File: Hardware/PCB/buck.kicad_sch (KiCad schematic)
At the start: 13 parts, among them J4 54-00127, U4 LMR33630BRNXR

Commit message: swapped to be better precision resistors for feedback on buck and votlage reference for ADCs
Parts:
- R10: footprint Capacitor_SMD:C_0402_1005Metric_Pad0.74x0.62mm_HandSolder -> Capacitor_SMD:C_0603_1608Metric_Pad1.08x0.95mm_HandSolder; DigiKey Link https://www.digikey.com/en/products/detail/yageo/RC0402FR-0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 -> https://www.digikey.com/en/products/detail/susumu/RG1608P-2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; MPN RC0402FR-0722K1L -> RG1608P-2212-B-T5; Manufacturer YAGEO -> Susumu
- R9: footprint Capacitor_SMD:C_0402_1005Metric_Pad0.74x0.62mm_HandSolder -> Capacitor_SMD:C_0603_1608Metric_Pad1.08x0.95mm_HandSolder; DigiKey Link https://www.digikey.com/en/products/detail/yageo/RC0402FR-0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 -> https://www.digikey.com/en/products/detail/susumu/RG1608P-1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; MPN RC0402FR-07100KL -> RG1608P-104-B-T5; Manufacturer YAGEO -> Susumu
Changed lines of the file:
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@@
 			)
 		)
-		(property "Footprint" "Capacitor_SMD:C_0402_1005Metric_Pad0.74x0.62mm_HandSolder"
+		(property "Footprint" "Capacitor_SMD:C_0603_1608Metric_Pad1.08x0.95mm_HandSolder"
 			(at 193.04 95.25 0)
 			(effects
@@
 			)
 		)
-		(property "Description" "100 kOhms ±1% 0.063W, 1/16W Chip Resistor 0402 (1005 Metric) Moisture Resistant Thick Film"
-			(at 193.04 95.25 0)
-			(effects
-				(font
-					(size 1.27 1.27)
-				)
-				(hide yes)
-			)
-		)
-		(property "DigiKey Link" "https://www.digikey.com/en/products/detail/yageo/RC0402FR-07100KL/726526"
-			(at 193.04 95.25 0)
-			(effects
-				(font
-					(size 1.27 1.27)
-				)
-				(hide yes)
-			)
-		)
-		(property "MPN" "RC0402FR-07100KL"
-			(at 193.04 95.25 0)
-			(effects
-				(font
-					(size 1.27 1.27)
-				)
-				(hide yes)
-			)
-		)
-		(property "Manufacturer" "YAGEO"
+		(property "Description" "100 kOhms ±0.1% 0.1W, 1/10W Chip Resistor 0603 (1608 Metric) Anti-Sulfur, Automotive AEC-Q200 Thin Film"
+			(at 193.04 95.25 0)
+			(effects
+				(font
+					(size 1.27 1.27)
+				)
+				(hide yes)
+			)
+		)
+		(property "DigiKey Link" "https://www.digikey.com/en/products/detail/susumu/RG1608P-104-B-T5/1240451"
+			(at 193.04 95.25 0)
+			(effects
+				(font
+					(size 1.27 1.27)
+				)
+				(hide yes)
+			)
+		)
+		(property "MPN" "RG1608P-104-B-T5"
+			(at 193.04 95.25 0)
+			(effects
+				(font
+					(size 1.27 1.27)
+				)
+				(hide yes)
+			)
+		)
+		(property "Manufacturer" "Susumu"
 			(at 193.04 95.25 0)
 			(effects
@@
 			)
 		)
-		(property "Footprint" "Capacitor_SMD:C_0402_1005Metric_Pad0.74x0.62mm_HandSolder"
+		(property "Footprint" "Capacitor_SMD:C_0603_1608Metric_Pad1.08x0.95mm_HandSolder"
 			(at 193.04 105.41 0)
 			(effects
@@
 			)
 		)
-		(property "Description" "22.1 kOhms ±1% 0.063W, 1/16W Chip Resistor 0402 (1005 Metric) Moisture Resistant Thick Film"
-			(at 193.04 105.41 0)
-			(effects
-				(font
-					(size 1.27 1.27)
-				)
-				(hide yes)
-			)
-		)
-		(property "DigiKey Link" "https://www.digikey.com/en/products/detail/yageo/RC0402FR-0722K1L/726563"
-			(at 193.04 105.41 0)
-			(effects
-				(font
-					(size 1.27 1.27)
-				)
-				(hide yes)
-			)
-		)
-		(property "MPN" "RC0402FR-0722K1L"
-			(at 193.04 105.41 0)
-			(effects
-				(font
-					(size 1.27 1.27)
-				)
-				(hide yes)
-			)
-		)
-		(property "Manufacturer" "YAGEO"
-			(at 193.04 105.41 0)
-			(effects
+		(property "Description" "22.1 kOhms ±0.1% 0.1W, 1/10W Chip Resistor 0603 (1608 Metric) Anti-Sulfur, Automotive AEC-Q200 Thin Film"
+			(at 193.04 105.41 0)
+			(effects
+				(font
+					(size 1.27 1.27)
+				)
+				(hide yes)
+			)
+		)
+		(property "DigiKey Link" "https://www.digikey.com/en/products/detail/susumu/RG1608P-2212-B-T5/1240513"
+			(at 193.04 105.41 0)
+			(effects
+				(font
+					(size 1.27 1.27)
+				)
+				(hide yes)
+			)
+		)
+		(property "MPN" "RG1608P-2212-B-T5"
+			(at 193.04 105.41 0)
+			(effects
+				(font
+					(size 1.27 1.27)
+				)
+				(hide yes)
+			)
+		)
+		(property "Manufacturer" "Susumu"
+			(at 193.04 105.41 0)
+			(effects

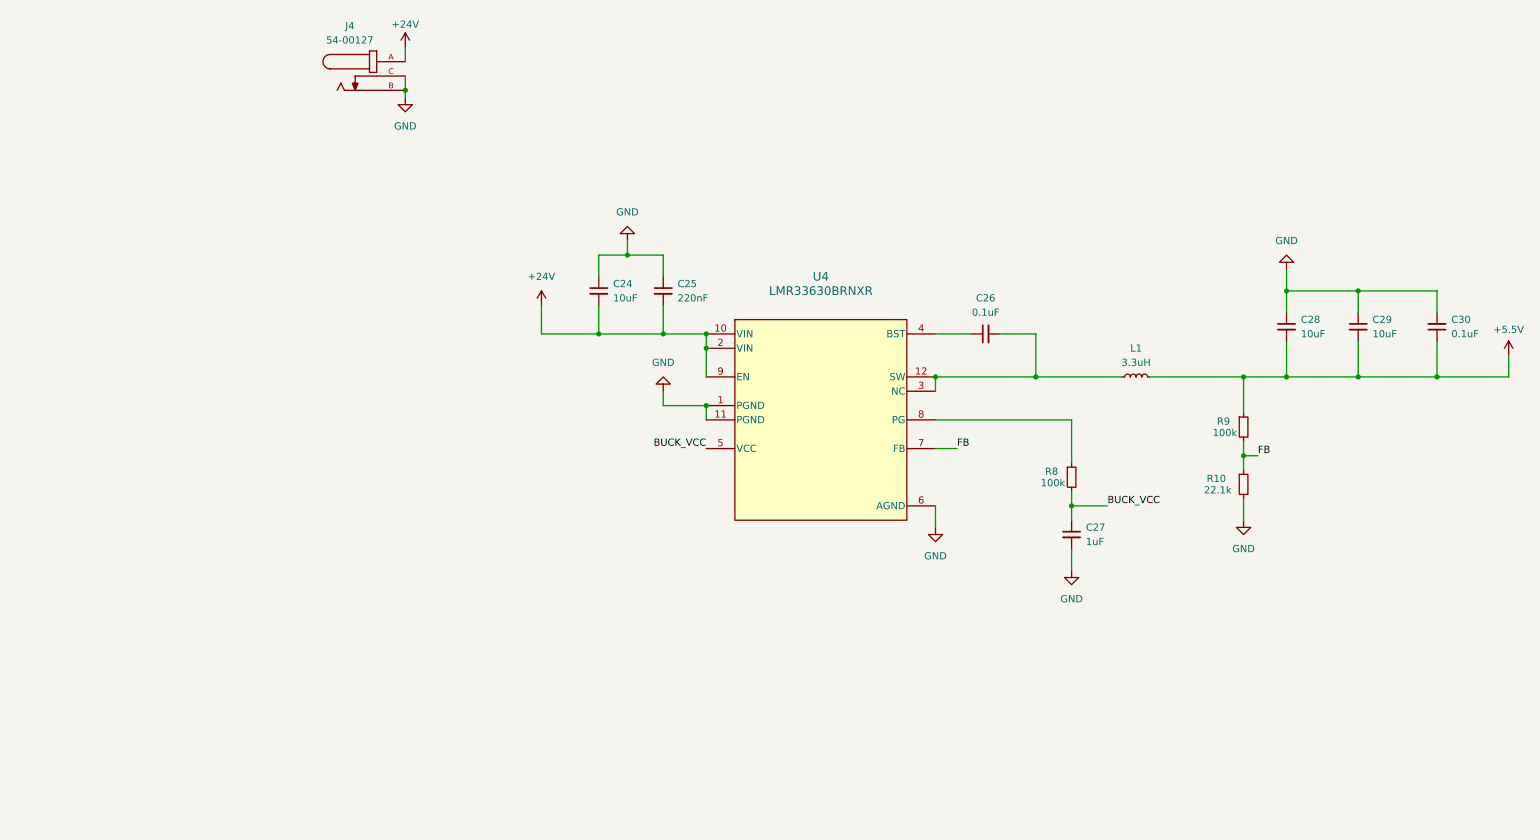
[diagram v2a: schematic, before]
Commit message: overall design is pretty much done, starting layout and routing now
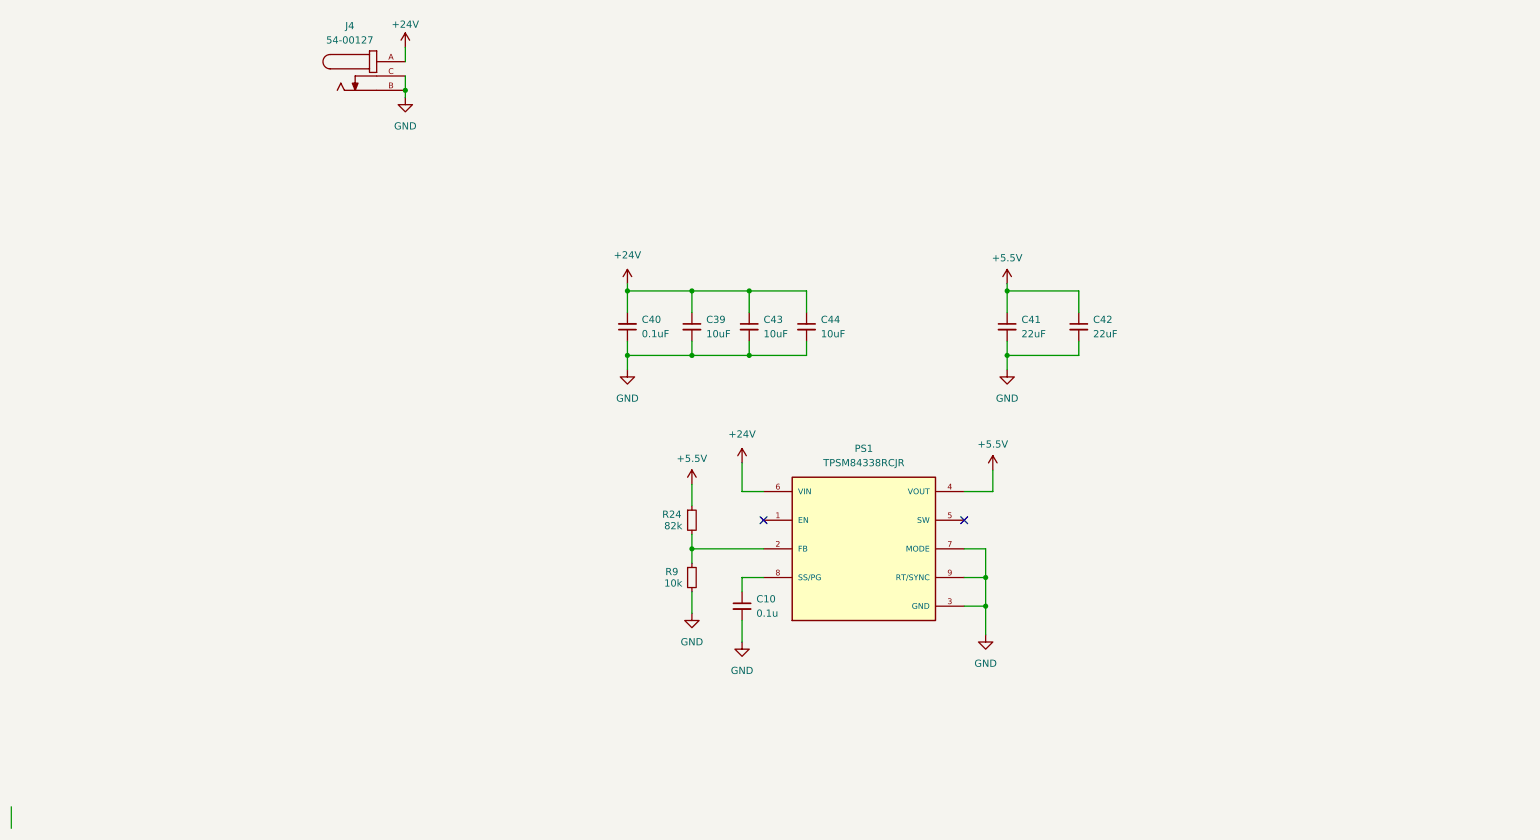
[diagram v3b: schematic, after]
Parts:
- removed C24, C28, C29: 10uF, Capacitor_SMD:C_1206_3216Metric_Pad1.33x1.80mm_HandSolder, symbol Device:C_Small
- removed C25: 220nF, Capacitor_SMD:C_0805_2012Metric_Pad1.18x1.45mm_HandSolder, symbol Device:C_Small
- removed C26, C30: 0.1uF, Capacitor_SMD:C_0805_2012Metric_Pad1.18x1.45mm_HandSolder, symbol Device:C_Small
- removed C27: 1uF, Capacitor_SMD:C_0603_1608Metric_Pad1.08x0.95mm_HandSolder, symbol Device:C_Small
- removed L1: 3.3uH, Inductor_SMD:L_Bourns_SRN8040TA, symbol Device:L_Small
- removed R10: 22.1k, Capacitor_SMD:C_0603_1608Metric_Pad1.08x0.95mm_HandSolder, symbol Device:R_Small
- removed R8: 100k, Capacitor_SMD:C_0402_1005Metric_Pad0.74x0.62mm_HandSolder, symbol Device:R_Small
- removed U4: LMR33630BRNXR, Vendor_Footprints:RNX0012B, symbol Vendor_Symbols:LMR33630BRNXR
- added C10: 0.1u, Capacitor_SMD:C_0603_1608Metric_Pad1.08x0.95mm_HandSolder, symbol Device:C_Small
- added C39, C43, C44: 10uF, Capacitor_SMD:C_1206_3216Metric_Pad1.33x1.80mm_HandSolder, symbol Device:C_Small
- added C40: 0.1uF, Capacitor_SMD:C_0603_1608Metric_Pad1.08x0.95mm_HandSolder, symbol Device:C_Small
- added C41, C42: 22uF, Capacitor_SMD:C_0805_2012Metric_Pad1.18x1.45mm_HandSolder, symbol Device:C_Small
- added PS1: TPSM84338RCJR, Vendor_Footprints:CONV_TPSM84338RCJR, symbol Vendor_Symbols:TPSM84338RCJR
- added R24: 82k, Capacitor_SMD:C_0603_1608Metric_Pad1.08x0.95mm_HandSolder, symbol Device:R_Small
- R9: value 100k -> 10k; DigiKey Link https://www.digikey.com/en/products/detail/susumu/RG1608P-1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 -> https://www.digikey.com/en/products/detail/susumu/RR0816P-1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; MPN RG1608P-104-B-T5 -> RR0816P-103-D
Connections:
- net FB is gone; now on net GND: R9.2
- net +24V: now also C39.1, C40.2, C43.1, C44.1, PS1.6 (VIN)
- net +5.5V: now also C41.1, C42.1, PS1.4 (VOUT), R24.1; no longer R9.1
- net GND: now also C10.2, C39.2, C40.1, C41.2, C42.2, C43.2, C44.2, PS1.3 (GND), PS1.7 (MODE), PS1.9 (RT/SYNC)
- new net: PS1.2 (FB), R24.2, R9.1
- new net: C10.1, PS1.8 (SS/PG)
- no-connect marks 0 -> 2
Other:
- moved on the sheet: R9

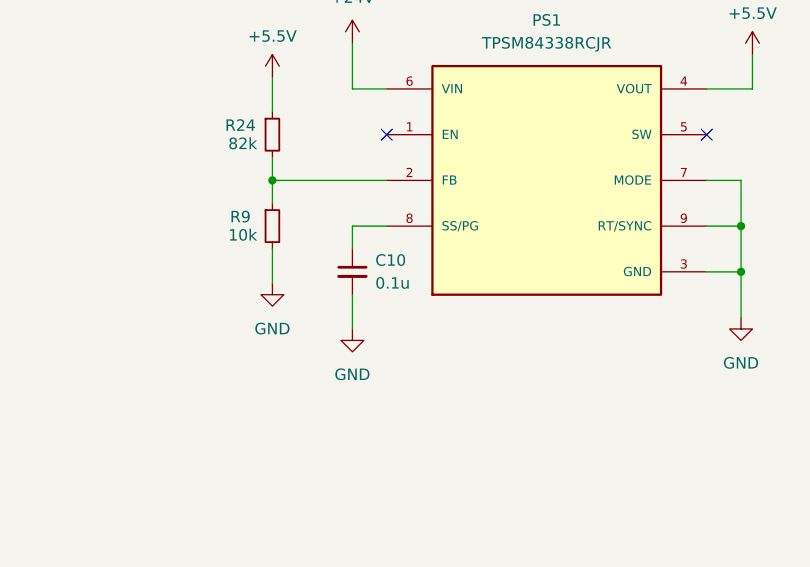
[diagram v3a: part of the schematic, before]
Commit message: fixed BOM, added some silkscreen, getting quote now
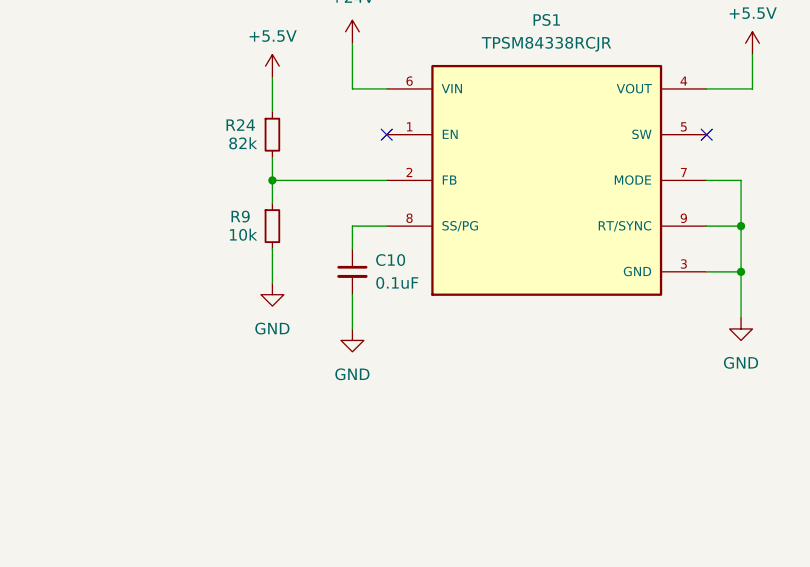
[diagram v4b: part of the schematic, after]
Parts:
- C10: value 0.1u -> 0.1uF
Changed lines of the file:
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@@
 			)
 		)
-		(property "Value" "0.1u"
+		(property "Value" "0.1uF"
 			(at 106.68 128.2762 0)
 			(effects

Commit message: kinda pricey, I should try to make a smaller version using LCSC parts for cheaper solution
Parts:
- C10: LCSC (none) -> C66501
- C39, C43, C44: LCSC (none) -> C13585
- C40: LCSC (none) -> C3011652; Manufacturer GCM188R71H104KA57J -> Murata Electronics
- C41, C42: LCSC (none) -> C398815
- J4: LCSC (none) -> C19856735
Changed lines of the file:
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@@
+			)
+		)
+		(property "LCSC" ""
+			(at 95.25 121.92 0)
+			(effects
+				(font
+					(size 1.27 1.27)
+				)
 			)
 		)
@@
 			)
 		)
+		(property "LCSC" ""
+			(at 125.73 116.84 0)
+			(effects
+				(font
+					(size 1.27 1.27)
+				)
+			)
+		)
 		(pin "4"
 		)
@@
 			)
 		)
+		(property "LCSC" "C13585"
+			(at 115.57 77.47 0)
+			(effects
+				(font
+					(size 1.27 1.27)
+				)
+			)
+		)
 		(pin "2"
 		)
@@
 			)
 		)
+		(property "LCSC" ""
+			(at 95.25 111.76 0)
+			(effects
+				(font
+					(size 1.27 1.27)
+				)
+			)
+		)
 		(pin "1"
 		)
@@
 			)
 		)
+		(property "LCSC" "C19856735"
+			(at 39.37 33.02 0)
+			(effects
+				(font
+					(size 1.27 1.27)
+				)
+			)
+		)
 		(pin "A"
 		)
@@
 			)
 		)
+		(property "LCSC" "C66501"
+			(at 104.14 127 0)
+			(effects
+				(font
+					(size 1.27 1.27)
+				)
+			)
+		)
 		(pin "2"
 		)
@@
 			)
 		)
+		(property "LCSC" "C13585"
+			(at 95.25 77.47 0)
+			(effects
+				(font
+					(size 1.27 1.27)
+				)
+			)
+		)
 		(pin "2"
 		)
@@
 			)
 		)
+		(property "LCSC" "C398815"
+			(at 151.13 77.47 0)
+			(effects
+				(font
+					(size 1.27 1.27)
+				)
+			)
+		)
 		(pin "2"
 		)
@@
 			)
 		)
+		(property "LCSC" "C13585"
+			(at 105.41 77.47 0)
+			(effects
+				(font
+					(size 1.27 1.27)
+				)
+			)
+		)
 		(pin "2"
 		)
@@
 			)
 		)
-		(property "Manufacturer" "GCM188R71H104KA57J"
+		(property "Manufacturer" "Murata Electronics"
 			(at 83.82 77.47 0)
 			(effects
@@
 				)
 				(hide yes)
+			)
+		)
+		(property "LCSC" "C3011652"
+			(at 83.82 77.47 0)
+			(effects
+				(font
+					(size 1.27 1.27)
+				)
 			)
 		)
@@
 			)
 		)
+		(property "LCSC" "C398815"
+			(at 163.83 77.47 0)
+			(effects
+				(font
+					(size 1.27 1.27)
+				)
+			)
+		)

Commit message: done with this, placed order
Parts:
- removed C10: 0.1uF, Capacitor_SMD:C_0603_1608Metric_Pad1.08x0.95mm_HandSolder, symbol Device:C_Small
- removed C41, C42: 22uF, Capacitor_SMD:C_0805_2012Metric_Pad1.18x1.45mm_HandSolder, symbol Device:C_Small
- removed C43, C44: 10uF, Capacitor_SMD:C_1206_3216Metric_Pad1.33x1.80mm_HandSolder, symbol Device:C_Small
- removed J4: 54-00127, Vendor_Footprints:TENSILITY_54-00127, symbol Vendor_Symbols:54-00127
- removed PS1: TPSM84338RCJR, Vendor_Footprints:CONV_TPSM84338RCJR, symbol Vendor_Symbols:TPSM84338RCJR
- removed R24: 82k, Capacitor_SMD:C_0603_1608Metric_Pad1.08x0.95mm_HandSolder, symbol Device:R_Small
- removed R9: 10k, Capacitor_SMD:C_0603_1608Metric_Pad1.08x0.95mm_HandSolder, symbol Device:R_Small
- added C18: 100nF, Capacitor_SMD:C_0603_1608Metric_Pad1.08x0.95mm_HandSolder, symbol Device:C_Small
- added C48, C49: 47uF, Capacitor_SMD:C_1210_3225Metric, symbol Device:C_Small
- added D8: SS310, Diode_SMD:D_SMA, symbol Device:D_Schottky
- added J6: XUNPU DC-005-A250, Connector_BarrelJack:BarrelJack_Horizontal, symbol Connector:Barrel_Jack_MountingPin
- added L1: 6.8uH, Inductor_SMD:L_Changjiang_FXL0630, symbol Device:L_Small
- added R10: 66.5k, Capacitor_SMD:C_0603_1608Metric_Pad1.08x0.95mm_HandSolder, symbol Device:R_Small
- added R27: 10.5k, Capacitor_SMD:C_0603_1608Metric_Pad1.08x0.95mm_HandSolder, symbol Device:R_Small
- added R28: 45.3k, Capacitor_SMD:C_0603_1608Metric_Pad1.08x0.95mm_HandSolder, symbol Device:R_Small
- added U9: LMR16030PDDAR, Vendor_Footprints:VREG_LM5017MR_NOPB, symbol Vendor_Symbols:LMR16030PDDAR
- C40: value 0.1uF -> 100nF; LCSC C3011652 -> C14663; MPN GCM188R71H104KA57J -> CC0603KRX7R9BB104; Manufacturer Murata Electronics -> YAGEO
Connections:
- net +24V: now also J6.1, U9.2 (VIN), U9.3 (EN)
- net +5.5V: now also C48.1, C49.1, L1.2, R10.1
- net GND: now also C48.2, C49.2, D8.2 (A), J6.2, J6.MP (MountPin), R27.2, R28.2, U9.7 (GND), U9.9 (THERMALPAD)
- new net: R28.1, U9.4 (RT/SYNC)
- new net: C18.2, D8.1 (K), L1.1, U9.8 (SW)
- new net: C18.1, U9.1 (BOOT)
- new net FB: R10.2, R27.1, U9.5 (FB)
- no-connect marks 2 -> 1
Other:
- moved on the sheet: C39, C40
